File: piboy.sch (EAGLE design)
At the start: 69 parts, among them CN4 MicroUSB, T1 MMUN2133LT1G, U1 TPS61090RSAR, U2 MCP73871, U3 TPA2005D1

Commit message: -finished the PAM8302A audio amp
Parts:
- removed C3, C5: 1uF, resistor:C-USC0805
- removed C9: 10uF, resistor:C-USC0805
- removed CMP_VIDEO_OUT, SPK1, SPK2: (no value), piboy_new:WIREPAD_1,6/0,9
- removed R10, R11: 150K, resistor:R-US_R0805
- removed R9: 10K, resistor:R-US_R0805
- removed U$33: RK10J12R0A0B, piboy_new:RK10J12R0A0B
- removed U$40: SJ-43504-SMT-TR, SJ-43504-SMT-TR:SJ-43504-SMT-TR
- removed U3: TPA2005D1, SparkFun-IC-Amplifiers:TPA2005D1DGN
- added C10: 33nF, resistor:C-USC0805
- added C11: 10uF, resistor:C-USC0805
- added C12, C13: 1uF, resistor:C-USC0805
- added C14: 100uF, resistor:C-USC1210
- added C15: 100nF, resistor:C-USC0805
- added C16, C17: 22pF, resistor:C-USC0805
- added CMP_VIDEO_OUT1, SPK3, SPK4: (no value), piboy_new:WIREPAD_1,6/0,9
- added FB1, FB2: (no value), Adafruit PAM8302:FERRITE0805
- added R12: 270, resistor:R-US_R0805
- added R15: 150, resistor:R-US_R0805
- added R18, R19: 100, resistor:R-US_R0805
- added R21: 10k, resistor:R-US_R0805
- added U$29: RK10J12R0A0B, piboy_new:RK10J12R0A0B
- added U$30: SJ-43504-SMT-TR, SJ-43504-SMT-TR:SJ-43504-SMT-TR
- added U4: (no value), Adafruit PAM8302:AUDIOAMP_PAM8302A
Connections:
- net 3.3V renamed +3.3V
- removed net 5.0V: BCM2,5.0V.P, C2.1, C6.1, C9.2, R3.2, R5.1, R9.1, U$9.P2, U$9.P4, U1.VOUT, U3.VDD
- removed net CMP_VIDEO_OUT: CMP_VIDEO_OUT.P, U$40.P$1
- removed net N$17: R9.2, U3.SHUTDOWN
- removed net N$20: C5.1, R10.2
- removed net N$21: C3.1, R11.2
- removed net N$22: R10.1, U$33.P$2
- removed net N$23: C5.2, U3.IN+
- removed net N$26: C3.2, U3.IN-
- new net +5V: BCM2,5.0V.P, C14.1, C15.1, C2.1, C6.1, R21.2, R3.2, R5.1, U$9.P2, U$9.P4, U1.VOUT, U4.VDD
- new net CMP_VIDEO_OUT1: CMP_VIDEO_OUT1.P, U$30.P$1
- new net N$18: C10.1, C11.1, R12.2
- new net N$35: C11.2, R15.2, U$29.P$3
- new net N$37: C12.1, U$29.P$2
- new net N$38: C13.1, U$29.P$1
- new net N$39: C13.2, R19.2
- new net N$40: C12.2, R18.2
- new net N$41: R18.1, U4.IN_P
- new net N$42: R19.1, U4.IN_N
- new net N$45: R21.1, U4./SD
- new net N$47: FB1.P$1, U4.VO_N
- new net N$48: FB2.P$1, U4.VO_P
- net AUD+: now also C17.1, FB2.P$2, U$30.P$2, U$30.P$3; no longer U$40.P$2, U$40.P$3, U3.OUT+
- net AUD+_HDPN_OUT: now also SPK4.P, U$30.P$5, U$30.P$6; no longer SPK2.P, U$40.P$5, U$40.P$6
- net AUD-: now also C16.1, FB1.P$2, SPK3.P, U$30.P$4; no longer SPK1.P, U$40.P$4, U3.OUT-
- net GND: now also C10.2, C14.2, C15.2, C16.2, C17.2, R15.1, U4.GND; no longer C9.1, R11.1, U$33.P$1, U3.GND@1, U3.GND@2
- net PWM0: now also R12.1; no longer U$33.P$3

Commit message: -did some wiring
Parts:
- C1, C7: device adafruit:C-USC0805 -> resistor:C-USC1210
- C6: device adafruit:C-USC1210 -> resistor:C-USC1210

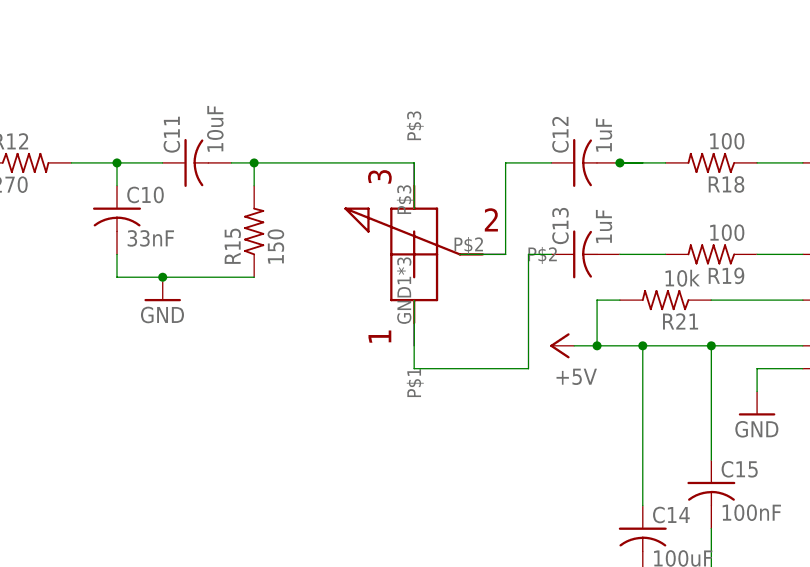
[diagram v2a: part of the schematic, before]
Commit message: -performed a DRC, no errors TODO fix silkscreen layers clean up wires
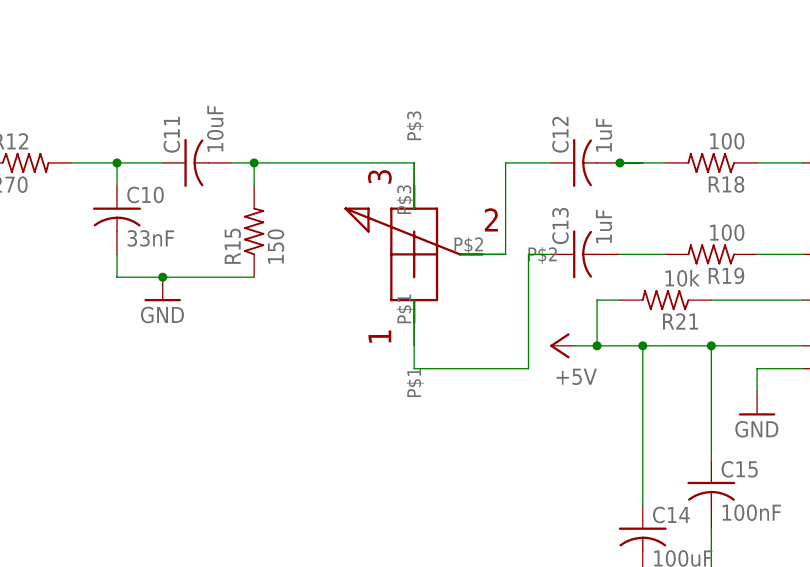
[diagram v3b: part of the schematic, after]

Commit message: -added license info on the schematic
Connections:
- net N$18: now also R15.2
- net N$35: no longer R15.2
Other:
- note added: "Audio Amplifier"
- note added: "Boost Circuitry (3.7V to 5.0V)"
- note added: "GPIO Header and SPI LCD Breakout"
- note added: "Li-Ion Charging Circuitry"
- note added: "License Info: Li-Ion Charging Circuitry and 3.7V Boost Circuitry are based on the PowerBoost 1000C Circuit By Adafruit. https://github.com/adafruit/Adafruit-PowerBoost-1000C Audio Amplifier Circuitry based on the PAM8302A Mono 2.5W Amplifier Circuit by Adafruit https://github.com/adafruit/Adafruit-PAM8302-Mono-Amplifier-PCB Circuit and PCB are licensed under Creative Commons Attribution Share-Ali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"
- note added: "PiBoy SP by Grant Haack https://www.granthaack.com/piboy-sp"
- note removed: "GPIO"
- note removed: "On/Off Switch"
- moved on the sheet: BCM1,3.3V, BCM18,GPIO24, BCM2,5.0V, BCM21,GPIO9, BCM22,GPIO25, BCM23,GPIO11, BCM24,GPIO8, BCM26,GPIO7, BCM27,ID_SD, BCM28,ID_SC, BCM6,GND, BVM19,GPIO10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

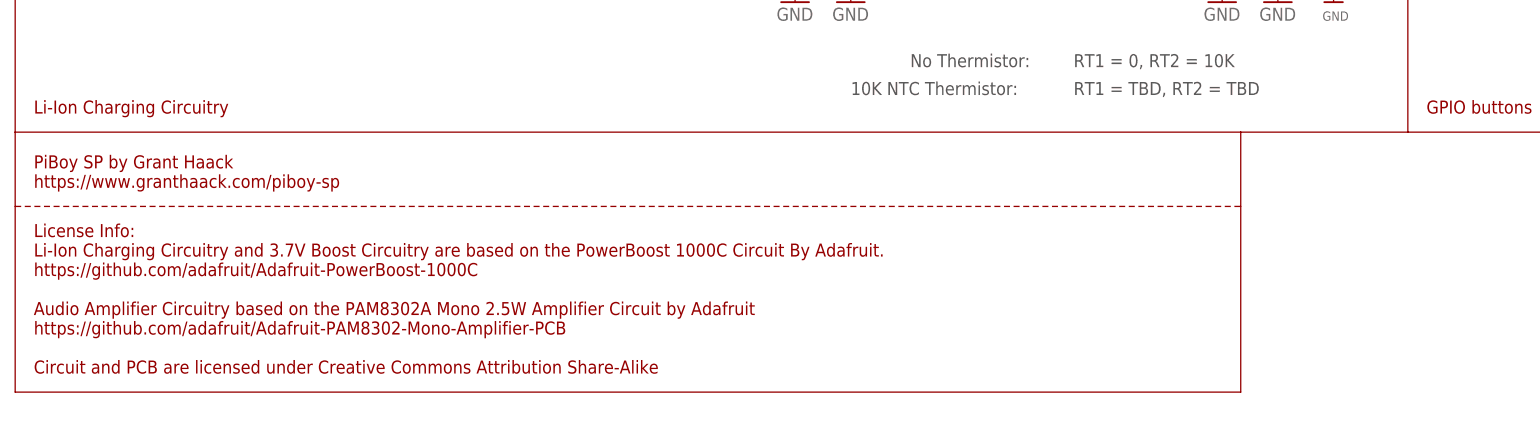
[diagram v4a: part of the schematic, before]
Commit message: -corrected license info
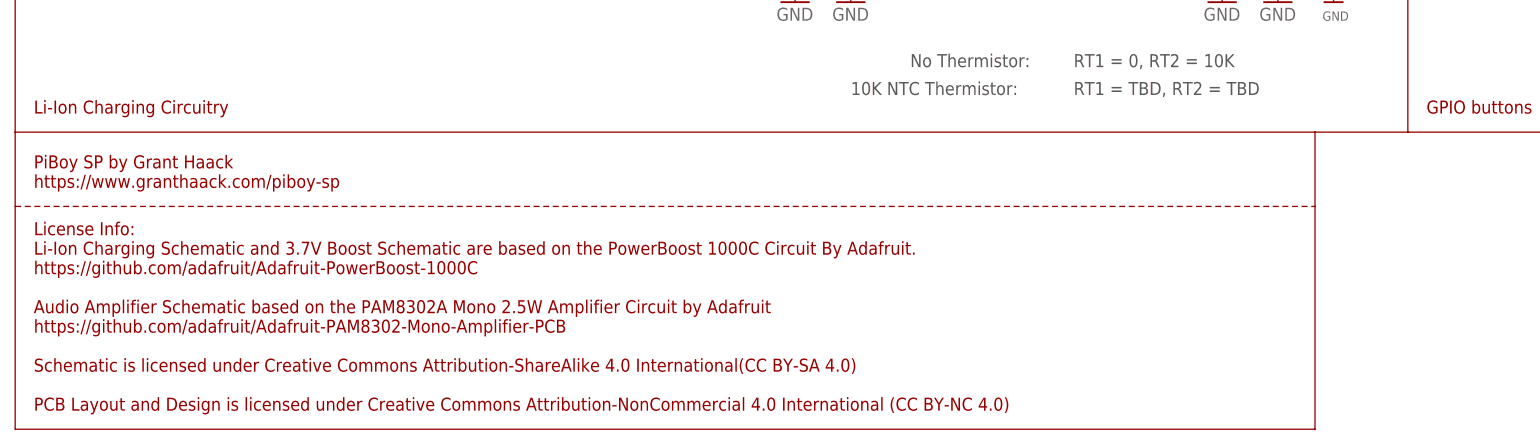
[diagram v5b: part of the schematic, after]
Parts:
- C11: device resistor:C-USC0805 -> resistor:C-USC1210
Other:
- note added: "License Info: Li-Ion Charging Schematic and 3.7V Boost Schematic are based on the PowerBoost 1000C Circuit By Adafruit. https://github.com/adafruit/Adafruit-PowerBoost-1000C Audio Amplifier Schematic based on the PAM8302A Mono 2.5W Amplifier Circuit by Adafruit https://github.com/adafruit/Adafruit-PAM8302-Mono-Amplifier-PCB Schematic is licensed under Creative Commons Attribution-ShareAlike 4.0 I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"
- note removed: "License Info: Li-Ion Charging Circuitry and 3.7V Boost Circuitry are based on the PowerBoost 1000C Circuit By Adafruit. https://github.com/adafruit/Adafruit-PowerBoost-1000C Audio Amplifier Circuitry based on the PAM8302A Mono 2.5W Amplifier Circuit by Adafruit https://github.com/adafruit/Adafruit-PAM8302-Mono-Amplifier-PCB Circuit and PCB are licensed under Creative Commons Attribution Share-Ali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"
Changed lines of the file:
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@@
 <part name="R12" library="resistor" library_urn="urn:adsk.eagle:library:348" deviceset="R-US_" device="R0805" package3d_urn="urn:adsk.eagle:package:26059/1" value="270"/>
 <part name="C10" library="resistor" library_urn="urn:adsk.eagle:library:348" deviceset="C-US" device="C0805" package3d_urn="urn:adsk.eagle:package:26137/1" value="33nF"/>
-<part name="C11" library="resistor" library_urn="urn:adsk.eagle:library:348" deviceset="C-US" device="C0805" package3d_urn="urn:adsk.eagle:package:26137/1" value="10uF"/>
+<part name="C11" library="resistor" library_urn="urn:adsk.eagle:library:348" deviceset="C-US" device="C1210" package3d_urn="urn:adsk.eagle:package:26139/1" value="10uF"/>
 <part name="R15" library="resistor" library_urn="urn:adsk.eagle:library:348" deviceset="R-US_" device="R0805" package3d_urn="urn:adsk.eagle:package:26059/1" value="150"/>
 <part name="GND26" library="supply1" deviceset="GND" device=""/>
@@
 <wire x1="215.9" y1="-165.1" x2="101.6" y2="-165.1" width="0.1524" layer="94"/>
 <wire x1="101.6" y1="-165.1" x2="-30.48" y2="-165.1" width="0.1524" layer="94"/>
-<wire x1="-30.48" y1="-165.1" x2="-53.34" y2="-165.1" width="0.1524" layer="94"/>
-<wire x1="-53.34" y1="-165.1" x2="-220.98" y2="-165.1" width="0.1524" layer="94"/>
+<wire x1="-30.48" y1="-165.1" x2="-43.18" y2="-165.1" width="0.1524" layer="94"/>
+<wire x1="-43.18" y1="-165.1" x2="-220.98" y2="-165.1" width="0.1524" layer="94"/>
 <wire x1="-220.98" y1="-165.1" x2="-220.98" y2="-73.66" width="0.1524" layer="94"/>
 <wire x1="-220.98" y1="-73.66" x2="-220.98" y2="48.26" width="0.1524" layer="94"/>
@@
 <text x="-218.44" y="-162.56" size="1.778" layer="94">Li-Ion Charging Circuitry</text>
 <text x="-27.94" y="-40.64" size="1.778" layer="94">Audio Amplifier</text>
-<text x="-218.44" y="-198.12" size="1.778" layer="94">License Info:
-Li-Ion Charging Circuitry and 3.7V Boost Circuitry are based on the PowerBoost 1000C Circuit By Adafruit.
+<text x="-218.44" y="-203.2" size="1.778" layer="94">License Info:
+Li-Ion Charging Schematic and 3.7V Boost Schematic are based on the PowerBoost 1000C Circuit By Adafruit.
 https://github.com/adafruit/Adafruit-PowerBoost-1000C
-Audio Amplifier Circuitry based on the PAM8302A Mono 2.5W Amplifier Circuit by Adafruit
+Audio Amplifier Schematic based on the PAM8302A Mono 2.5W Amplifier Circuit by Adafruit
 https://github.com/adafruit/Adafruit-PAM8302-Mono-Amplifier-PCB
-Circuit and PCB are licensed under Creative Commons Attribution Share-Alike</text>
+Schematic is licensed under Creative Commons Attribution-ShareAlike 4.0 International(CC BY-SA 4.0)
+PCB Layout and Design is licensed under Creative Commons Attribution-NonCommercial 4.0 International (CC BY-NC 4.0)</text>
 <text x="-218.44" y="-172.72" size="1.778" layer="94">PiBoy SP by Grant Haack
 https://www.granthaack.com/piboy-sp</text>
 <wire x1="-220.98" y1="-165.1" x2="-220.98" y2="-175.26" width="0.1524" layer="94"/>
-<wire x1="-220.98" y1="-175.26" x2="-220.98" y2="-200.66" width="0.1524" layer="94"/>
-<wire x1="-220.98" y1="-200.66" x2="-53.34" y2="-200.66" width="0.1524" layer="94"/>
-<wire x1="-53.34" y1="-200.66" x2="-53.34" y2="-175.26" width="0.1524" layer="94"/>
-<wire x1="-53.34" y1="-175.26" x2="-53.34" y2="-165.1" width="0.1524" layer="94"/>
-<wire x1="-220.98" y1="-175.26" x2="-53.34" y2="-175.26" width="0.1524" layer="94" style="shortdash"/>
+<wire x1="-220.98" y1="-175.26" x2="-220.98" y2="-205.74" width="0.1524" layer="94"/>
+<wire x1="-220.98" y1="-205.74" x2="-43.18" y2="-205.74" width="0.1524" layer="94"/>
+<wire x1="-43.18" y1="-205.74" x2="-43.18" y2="-175.26" width="0.1524" layer="94"/>
+<wire x1="-43.18" y1="-175.26" x2="-43.18" y2="-165.1" width="0.1524" layer="94"/>
+<wire x1="-220.98" y1="-175.26" x2="-43.18" y2="-175.26" width="0.1524" layer="94" style="shortdash"/>
 </plain>
 <instances>

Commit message: -added safe shutdown circuit
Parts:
- removed ON/OFF: (no value), piboy_new:ADAFRUIT_EG1218S
- added R10: 100K, adafruit:R-US_R0805
- added U$31: EG2210-SW, piboy_new:EG2210-SW
- added U$40: MMBF5460, piboy_new:MMBF5460
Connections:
- new net KEEPALIVE: R10.2, U$40.G, U$9.P3
- new net N$20: U$31.P$3
- new net N$21: U$31.P$1, U$40.D
- new net SHUTDOWN: U$31.P$4, U$9.P40
- net +3.3V: now also U$31.P$5
- net ENABLE: now also U$31.P$2; no longer ON/OFF.P
- net GND: now also R10.1, U$31.GND, U$40.S; no longer ON/OFF.O
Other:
- moved on the sheet: C1, C2, C4, C6, L1, LBO, ON, R1, R13, R2, R20, R3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
